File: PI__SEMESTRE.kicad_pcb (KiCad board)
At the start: 2 copper layers, 32 parts, among them IC2 LMV358IDR, J1 CX90B-16P1, U1 ESP32-S3-WROOM-1, U2 AMS1117, U5 GUVA-S12SD, U6 BME688

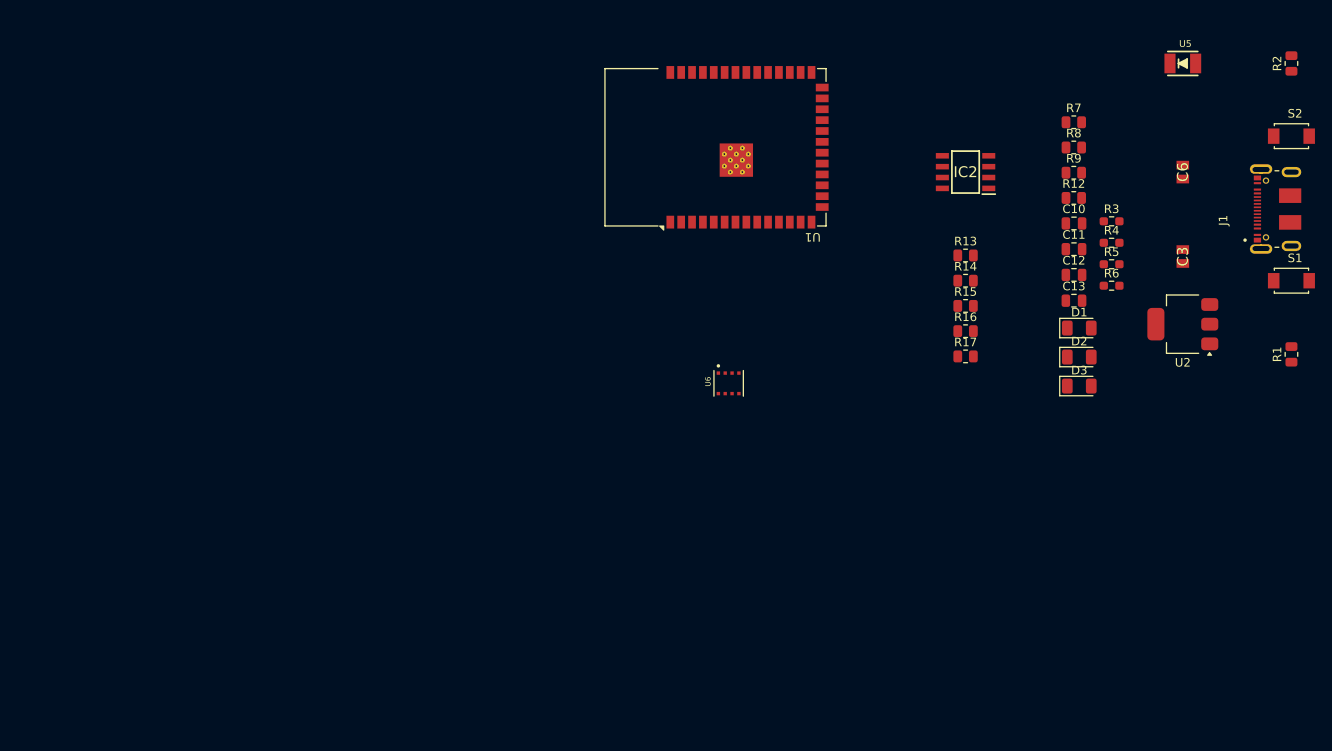
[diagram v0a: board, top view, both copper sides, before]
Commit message: se empieza a realizar el diseño para la pcb se dejan los componentes pocisionados para luego hacer las pistas, se rellena el contorno de la placa con conexion GND.
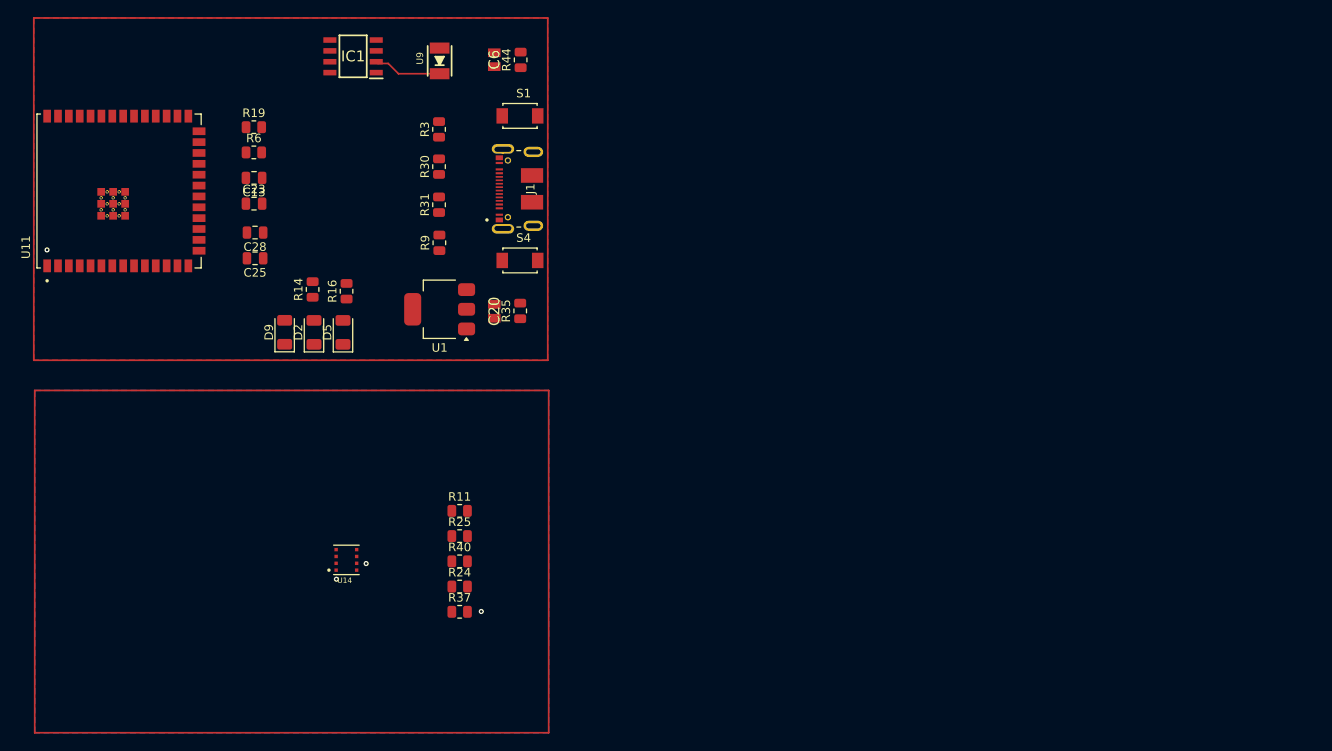
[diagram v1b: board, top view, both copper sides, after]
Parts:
- removed R4: 22Ω, Resistor_SMD:R_0603_1608Metric_Pad0.98x0.95mm_HandSolder
- removed R5: 10KΩ, Resistor_SMD:R_0603_1608Metric_Pad0.98x0.95mm_HandSolder
- removed the R6 at (194.9, 89.5)
- removed the U1 at (148.5, 73.3)
- added R30: 22Ω, Resistor_SMD:R_0805_2012Metric, F.Cu at (116.2, 75.6)
- added R31: 22Ω, Resistor_SMD:R_0805_2012Metric, F.Cu at (116.2, 80.0)
- added R9: 10KΩ, Resistor_SMD:R_0805_2012Metric, F.Cu at (116.3, 84.5)
- added U11: ESP32-S3-WROOM-1, SamacSys_Parts:XCVR_ESP32-S3-WROOM-1U-N16R8, F.Cu at (78.8, 78.4)
- R3: value 22Ω -> 10KΩ; footprint Resistor_SMD:R_0603_1608Metric_Pad0.98x0.95mm_HandSolder -> Resistor_SMD:R_0805_2012Metric
- moved C28 96.1 mm to (94.7, 83.3), turned to 180 degrees
- moved R19 96.0 mm to (94.6, 71.0)
- moved R6 96.0 mm to (94.6, 73.9)
- moved C13 96.0 mm to (94.6, 76.9), turned to 180 degrees
- moved C23 96.0 mm to (94.6, 79.9)
- moved C25 95.8 mm to (94.7, 86.3), turned to 180 degrees
- moved D9 93.1 mm to (98.2, 94.9), turned to 90 degrees
- moved R14 91.1 mm to (101.5, 89.9), turned to 90 degrees
- moved R35 90.3 mm to (125.7, 92.4)
- moved S1 90.2 mm to (125.7, 69.6)
- moved S4 90.2 mm to (125.7, 86.5)
- moved R44 90.1 mm to (125.8, 63.1)
- moved D2 89.5 mm to (101.6, 94.9), turned to 90 degrees
- moved J1 88.7 mm to (126.9, 78.2)
- moved U1 86.9 mm to (116.3, 92.2)
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- renumbered C10 to C13, C3 to C20, C11 to C23, C12 to C25, C13 to C28, D1 to D2, D2 to D5, D3 to D9, IC2 to IC1, R13 to R11, R7 to R14, R8 to R16, R9 to R19, R16 to R24, R14 to R25, R1 to R35, R17 to R37, R15 to R40, R2 to R44, R12 to R6, S2 to S1, S1 to S4, U2 to U1, U6 to U14, U5 to U9
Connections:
- R3 pad 1: Net-(U1-USB_D+) -> +3.3V
- R3 pad 2: D+ -> Boot
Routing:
- net Net-(IC1-1IN-): track 0.00 -> 7.99 mm
- net GND: vias 0 -> 4
- added copper zone on B.Cu, net GND
- added copper zone on F.Cu, net GND

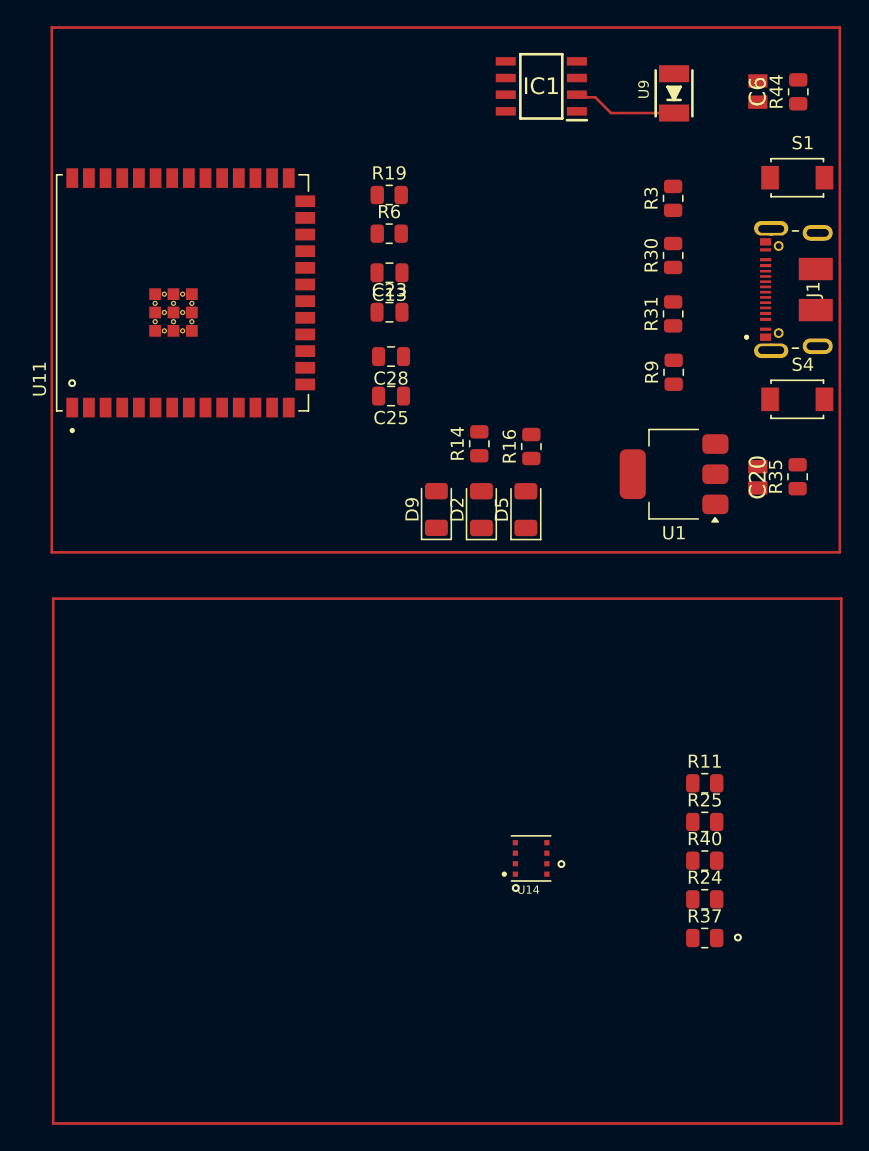
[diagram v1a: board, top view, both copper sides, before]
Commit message: se colocan algunas pistas de potencia, se unifican las dos capas en una misma pcb se hace pruebas de tamaños
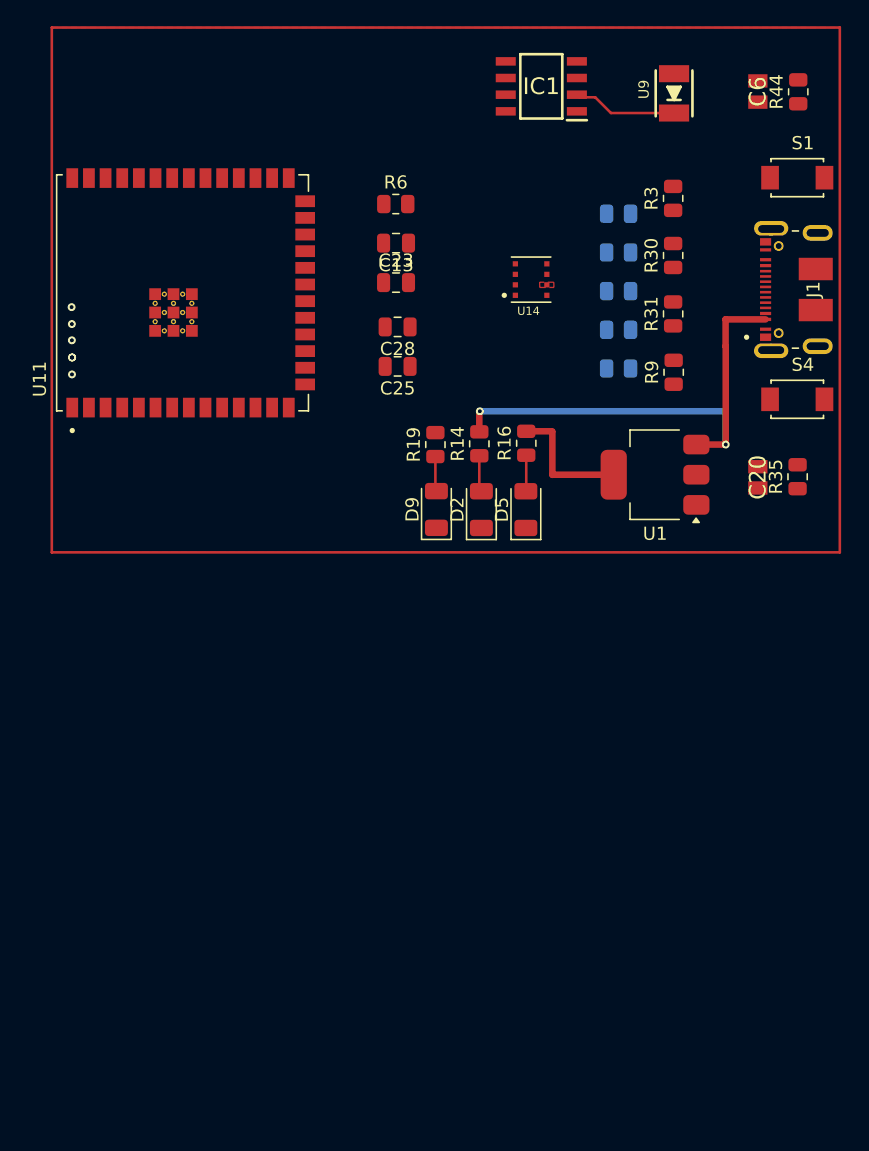
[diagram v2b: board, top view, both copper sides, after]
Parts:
- R11, R24, R25, R37, R40: moved to B.Cu
- moved U14 44.1 mm to (105.4, 77.4)
- moved R11 43.9 mm to (112.1, 72.4), turned to 180 degrees
- moved R25 43.9 mm to (112.1, 75.3), turned to 180 degrees
- moved R24 43.9 mm to (112.1, 81.2), turned to 180 degrees
- moved R37 43.9 mm to (112.1, 84.2), turned to 180 degrees
- moved R40 43.9 mm to (112.1, 78.3), turned to 180 degrees
- moved R19 19.4 mm to (98.1, 90.0), turned to 90 degrees
- moved C23 2.31 mm to (95.1, 77.6)
- moved C25 2.31 mm to (95.2, 84.0)
- moved R6 2.31 mm to (95.1, 71.6)
- moved C13 2.31 mm to (95.1, 74.6)
- moved C28 2.31 mm to (95.2, 81.0)
- moved U1 1.45 mm to (114.9, 92.3)
- moved R16 0.46 mm to (105.0, 89.9)
- turned C20 to -90 degrees
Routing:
- net +5V: track 0.00 -> 37.8 mm, vias 0 -> 2
- net +3.3V: track 0.00 -> 10.0 mm
- net Net-(D5-A): track 0.00 -> 3.35 mm
- net Net-(D2-A): track 0.00 -> 2.77 mm
- net Net-(D9-A): track 0.00 -> 2.67 mm
- net GND: vias 4 -> 6

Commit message: Se deja ya lista la pcb para que el profesor pase revision y noos indique los errores a corregir
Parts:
- moved C25 23.0 mm to (91.7, 61.3), turned to 90 degrees
- moved C28 19.7 mm to (94.7, 61.3), turned to 90 degrees
- moved R6 17.3 mm to (111.9, 67.4), turned to 90 degrees
- moved C13 13.2 mm to (106.5, 68.1), turned to 90 degrees
- moved C23 12.7 mm to (103.5, 68.1), turned to -90 degrees
- moved U14 4.98 mm to (100.5, 78.2)
- turned C6 to 90 degrees
- turned R40 to 0 degrees
- turned R44 to -90 degrees
- turned R9 to -90 degrees
- turned U9 to 0 degrees
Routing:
- net +3.3V: track 10.0 -> 158.9 mm, vias 0 -> 4
- net ADC ESP32: track 0.00 -> 83.1 mm, vias 0 -> 2
- net EN: track 0.00 -> 75.8 mm, vias 0 -> 2
- net I2C_SDA: track 0.00 -> 61.7 mm, vias 0 -> 1
- net I2C_SCL: track 0.00 -> 58.7 mm, vias 0 -> 1
- net Net-(U11-USB_D-): track 0.00 -> 41.1 mm, vias 0 -> 2
- net Net-(J1-CC1): track 0.00 -> 38.7 mm, vias 0 -> 2
- net Net-(U11-USB_D+): track 0.00 -> 37.6 mm, vias 0 -> 2
- net /filtro: track 0.00 -> 35.0 mm, vias 0 -> 2
- net Net-(U14-SDO): track 0.00 -> 25.8 mm, vias 0 -> 1
- net Net-(J1-CC2): track 0.00 -> 23.2 mm, vias 0 -> 2
- net Net-(U14-CSB): track 0.00 -> 20.6 mm, vias 0 -> 1
- net +5V: track 37.8 -> 58.0 mm, vias 2 -> 4
- net D-: track 0.00 -> 19.2 mm
- net Boot: track 0.00 -> 14.7 mm
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
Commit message: algunas correcciones del profesor
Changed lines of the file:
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@@
-	)
-	(segment
-		(start 96.28 78.55)
-		(end 96.25 78.58)
-		(width 0.2)
-		(layer "F.Cu")
-		(net "Net-(U14-CSB)")
-	)
-	(segment
-		(start 96.25 78.58)
-		(end 96.25 81.25)
-		(width 0.2)
-		(layer "F.Cu")
-		(net "Net-(U14-CSB)")
 	)
 	(segment
 		(start 99.285 78.55)
-		(end 96.28 78.55)
+		(end 96.6216 78.5368)
 		(width 0.2)
 		(layer "F.Cu")
@@
 		(start 96.25 81.25)
 		(end 106.39 81.25)
+		(width 0.2)
+		(layer "F.Cu")
+		(net "Net-(U14-CSB)")
+	)
+	(segment
+		(start 96.266 78.9178)
+		(end 96.25 81.25)
+		(width 0.2)
+		(layer "F.Cu")
+		(net "Net-(U14-CSB)")
+	)
+	(segment
+		(start 96.6216 78.5368)
+		(end 96.266 78.9178)
 		(width 0.2)
 		(layer "F.Cu")
@@
 	)
 	(segment
-		(start 107.33 82.9)
-		(end 94.84 82.9)
-		(width 0.2)
-		(layer "F.Cu")
-		(net "I2C_SDA")
-	)
-	(segment
-		(start 107.32 78.4)
-		(end 107.32 82.89)
+		(start 107.3658 82.423)
+		(end 106.8324 82.9564)
 		(width 0.2)
 		(layer "F.Cu")
@@
 	)
 	(segment
-		(start 107.32 82.89)
-		(end 107.33 82.9)
+		(start 107.32 78.4)
+		(end 107.3658 82.423)
 		(width 0.2)
 		(layer "F.Cu")
@@
 	)
 	(segment
+		(start 94.7674 82.3722)
+		(end 94.84 77.9)
+		(width 0.2)
+		(layer "F.Cu")
+		(net "I2C_SDA")
+	)
+	(segment
 		(start 79.3 90.41)
 		(end 90.91 90.41)
+		(width 0.2)
+		(layer "F.Cu")
+		(net "I2C_SDA")
+	)
+	(segment
+		(start 106.8324 82.9564)
+		(end 95.1992 82.931)
 		(width 0.2)
 		(layer "F.Cu")
@@
 	)
 	(segment
-		(start 94.84 82.9)
-		(end 94.84 77.9)
+		(start 95.1992 82.931)
+		(end 94.7674 82.3722)
 		(width 0.2)
 		(layer "F.Cu")

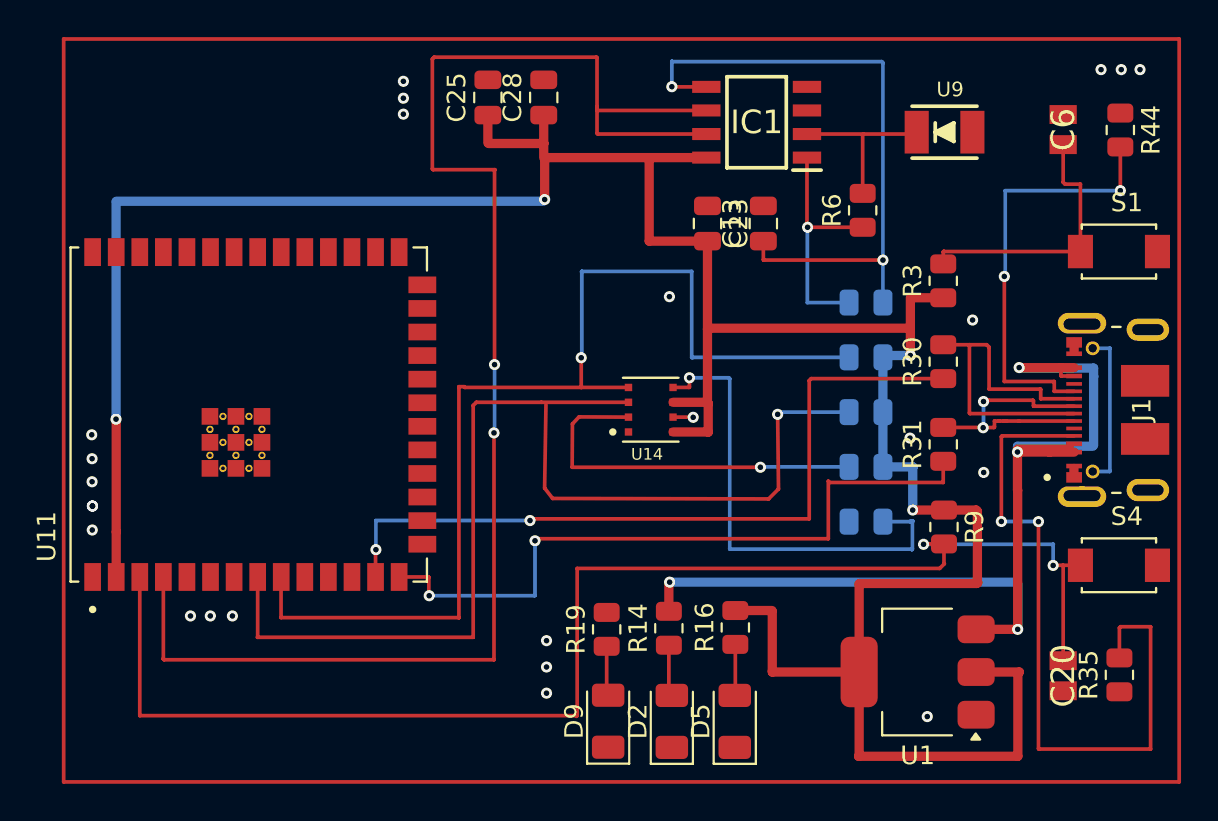
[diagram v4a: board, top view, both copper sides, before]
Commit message: se hacen los cambios de las pistas esquineras de (90 Grados) a curvas de (45 Grados) estos cambios solamente se le hicieron a las pistas azules, se le agrega la conexion del led faltante del (ESP) para nuestro KEEP ALIVE, se hace la conexion a algunas pistas faltantes que no se veian que habian por conectar, correciones de algunos GND sin conexion.
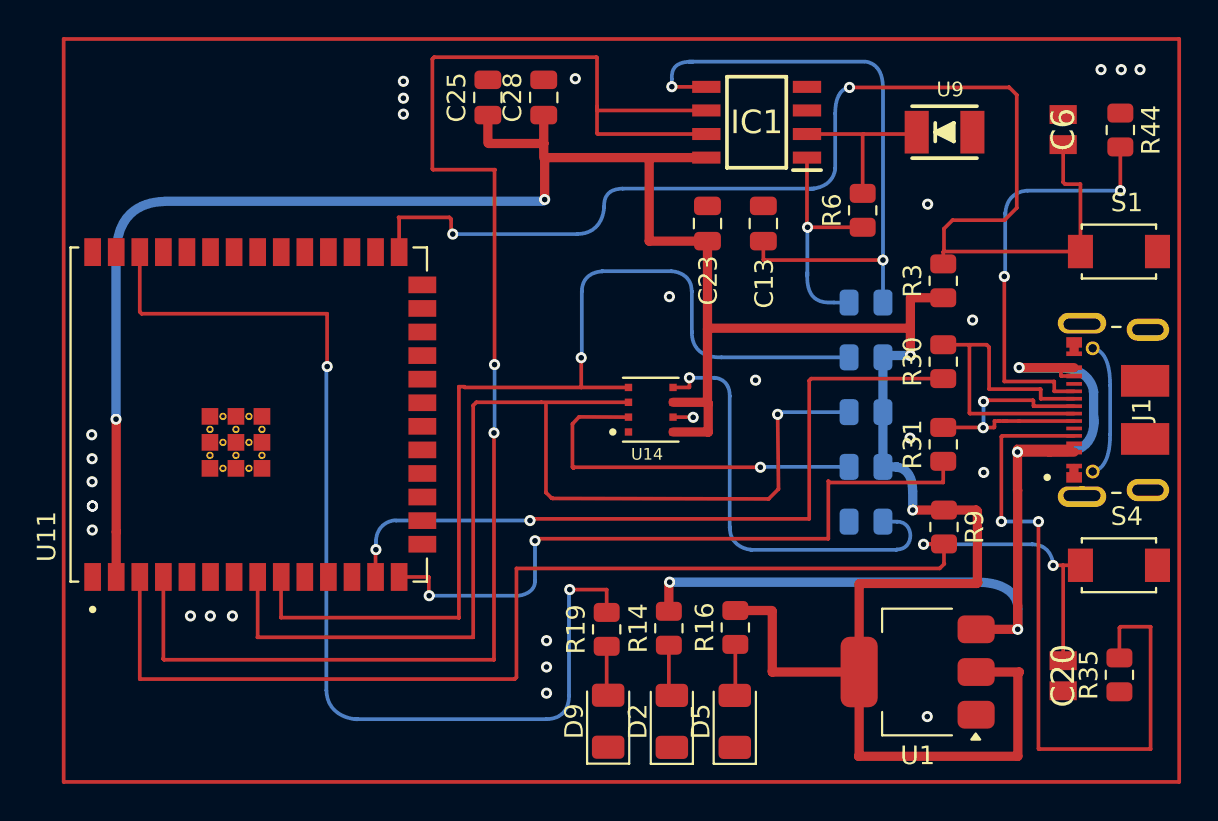
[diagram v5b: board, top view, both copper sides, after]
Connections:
- net /filtro renamed Filtro
- R19 pad 2: unconnected-(R19-Pad2) -> GPIO2
- U11 pad 38: unconnected-(U11-IO2-Pad38) -> GPIO2
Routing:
- net GPIO2: track 0.00 -> 53.0 mm, vias 0 -> 2
- net Boot: track 14.7 -> 61.2 mm, vias 0 -> 2
- net +5V: track 58.0 -> 47.9 mm
- net +3.3V: track 158.9 -> 151.3 mm
- net I2C_SCL: track 58.7 -> 51.4 mm
- net Net-(U14-SDO): track 25.8 -> 18.5 mm
- net EN: track 75.8 -> 69.5 mm
- net Net-(J1-MID_PLATE-PadMID1): track 8.49 -> 2.65 mm
- net Filtro: track 35.0 -> 30.7 mm
- net Net-(IC1-OUT): track 13.1 -> 10.2 mm
- net Net-(J1-CC2): track 23.2 -> 20.8 mm
- net Net-(U11-USB_D-): track 41.1 -> 38.9 mm
- net Net-(U11-USB_D+): track 37.6 -> 35.8 mm
- net GND: vias 24 -> 27
